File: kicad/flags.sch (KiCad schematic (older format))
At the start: 3 parts, among them U48 74LS173

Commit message: bugfixed design
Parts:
- renumbered U48 to U47
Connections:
- wire segments 27 -> 24
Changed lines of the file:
@@
 LIBS:valves
 LIBS:switches
-LIBS:74xxx
-LIBS:28c16
 LIBS:sap-be-cache
-EELAYER 24 0
+EELAYER 25 0
 EELAYER END
 $Descr A4 11693 8268
@@
 ZF
 $Comp
-L 74LS173 U48
+L 74LS173 U47
 U 1 1 5AD47646
 P 3600 2050
-F 0 "U48" H 3700 2150 50  0000 C CNN
+F 0 "U47" H 3700 2150 50  0000 C CNN
 F 1 "74LS173" H 3700 2000 50  0000 C CNN
 F 2 "" H 3600 2050 50  0000 C CNN
@@
 ~LOAD
 $Comp
-L GND #PWR090
+L GND #PWR88
 U 1 1 5AD4767C
 P 2450 2100
-F 0 "#PWR090" H 2450 1850 50  0001 C CNN
+F 0 "#PWR88" H 2450 1850 50  0001 C CNN
 F 1 "GND" H 2450 1950 50  0000 C CNN
 F 2 "" H 2450 2100 50  0000 C CNN
@@
 	1550 950  1300 950
 Wire Wire Line
-	2550 2300 2800 2300
-Wire Wire Line
-	2800 2300 2900 2300
+	2550 2300 2900 2300
 Wire Wire Line
 	2800 2300 2800 2200
@@
 Connection ~ 2800 2300
 Wire Wire Line
-	2900 2050 2800 2050
-Wire Wire Line
-	2800 2050 2450 2050
+	2450 2050 2900 2050
 Wire Wire Line
 	2450 2050 2450 2100
@@
 $EndComp
 $Comp
-L GND #PWR091
+L GND #PWR89
 U 1 1 5AD4AD59
 P 5600 2100
-F 0 "#PWR091" H 5600 1850 50  0001 C CNN
+F 0 "#PWR89" H 5600 1850 50  0001 C CNN
 F 1 "GND" H 5600 1950 50  0000 C CNN
 F 2 "" H 5600 2100 50  0000 C CNN
@@
 	5600 2100 5600 2050
 Wire Wire Line
-	5450 2050 5600 2050
-Wire Wire Line
-	5600 2050 5750 2050
+	5450 2050 5750 2050
 Wire Wire Line
 	5450 2050 5450 1950

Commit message: design as built
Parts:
- D601: renamed from D68; footprint (none) -> LEDs:LED-5MM
- D602: renamed from D69; footprint (none) -> LEDs:LED-5MM
- U601: renamed from U47; footprint (none) -> Housings_DIP:DIP-16_W7.62mm_LongPads
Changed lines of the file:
@@
 LIBS:valves
 LIBS:switches
+LIBS:74xxx
+LIBS:28c16
+LIBS:ne556
 LIBS:sap-be-cache
 EELAYER 25 0
@@
 Sheet 12 12
 Title "Simple As Possible computer by Ben Eater"
-Date "2017-05-10"
-Rev "1"
+Date "2018-06-03"
+Rev "2"
 Comp "Schematic released as CC BY-SA"
 Comment1 "Schematic capture by Vincent Sanders"
@@
 ZF
 $Comp
-L 74LS173 U47
+L 74LS173 U601
 U 1 1 5AD47646
 P 3600 2050
-F 0 "U47" H 3700 2150 50  0000 C CNN
+F 0 "U601" H 3700 2150 50  0000 C CNN
 F 1 "74LS173" H 3700 2000 50  0000 C CNN
-F 2 "" H 3600 2050 50  0000 C CNN
+F 2 "Housings_DIP:DIP-16_W7.62mm_LongPads" H 3600 2050 50  0001 C CNN
 F 3 "" H 3600 2050 50  0000 C CNN
 	1    3600 2050
@@
 ~LOAD
 $Comp
-L GND #PWR88
+L GND #PWR034
 U 1 1 5AD4767C
 P 2450 2100
-F 0 "#PWR88" H 2450 1850 50  0001 C CNN
+F 0 "#PWR034" H 2450 1850 50  0001 C CNN
 F 1 "GND" H 2450 1950 50  0000 C CNN
 F 2 "" H 2450 2100 50  0000 C CNN
@@
 NoConn ~ 2900 1800
 $Comp
-L LED D68
+L LED D601
 U 1 1 5AD4AD3C
 P 5450 1800
-F 0 "D68" H 5450 1900 50  0000 C CNN
+F 0 "D601" H 5450 1900 50  0000 C CNN
 F 1 "LED" H 5450 1700 50  0000 C CNN
-F 2 "" H 5450 1800 50  0000 C CNN
+F 2 "LEDs:LED-5MM" H 5450 1800 50  0001 C CNN
 F 3 "" H 5450 1800 50  0000 C CNN
 	1    5450 1800
@@
 $EndComp
 $Comp
-L LED D69
+L LED D602
 U 1 1 5AD4AD4E
 P 5750 1800
-F 0 "D69" H 5750 1900 50  0000 C CNN
+F 0 "D602" H 5750 1900 50  0000 C CNN
 F 1 "LED" H 5750 1700 50  0000 C CNN
-F 2 "" H 5750 1800 50  0000 C CNN
+F 2 "LEDs:LED-5MM" H 5750 1800 50  0001 C CNN
 F 3 "" H 5750 1800 50  0000 C CNN
 	1    5750 1800
@@
 $EndComp
 $Comp
-L GND #PWR89
+L GND #PWR035
 U 1 1 5AD4AD59
 P 5600 2100
-F 0 "#PWR89" H 5600 1850 50  0001 C CNN
+F 0 "#PWR035" H 5600 1850 50  0001 C CNN
 F 1 "GND" H 5600 1950 50  0000 C CNN
 F 2 "" H 5600 2100 50  0000 C CNN

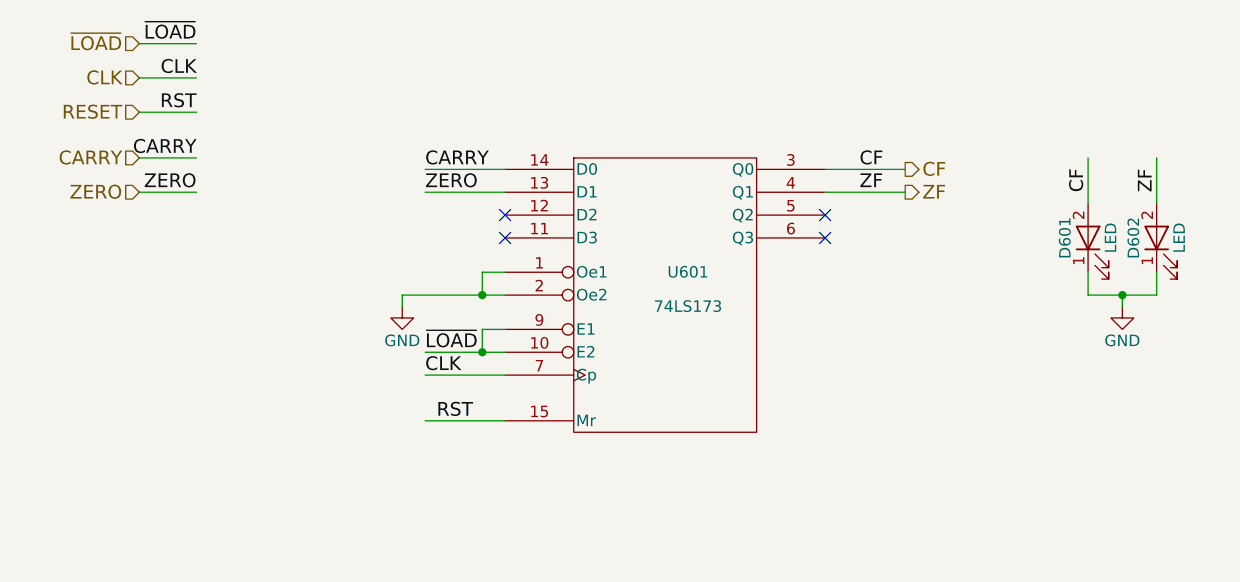
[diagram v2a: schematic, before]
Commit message: Update to current kicad version
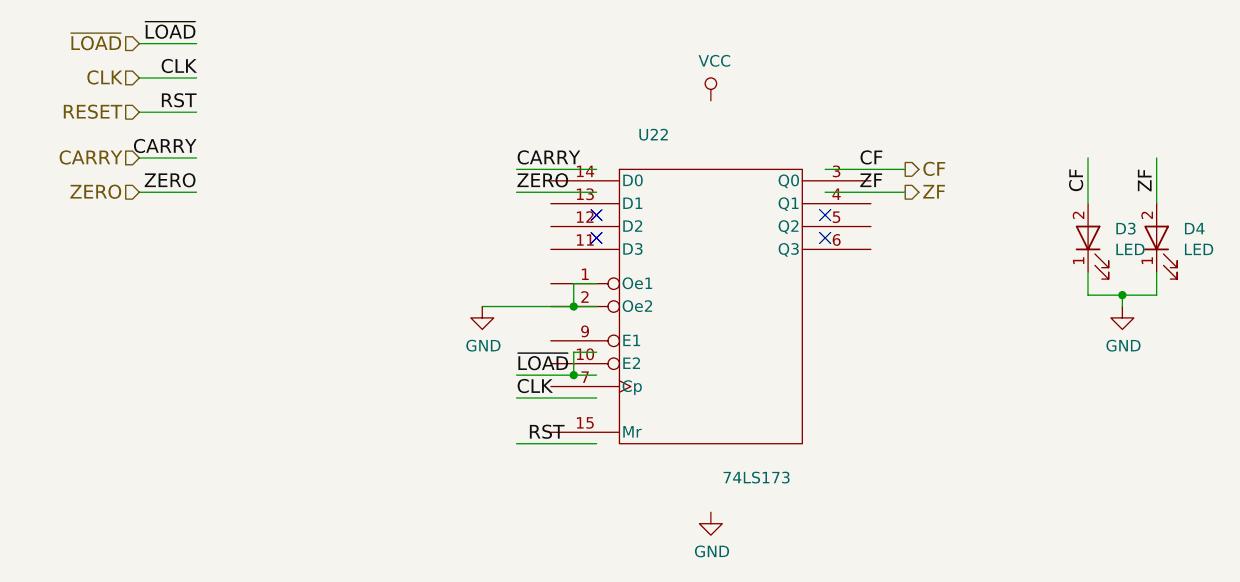
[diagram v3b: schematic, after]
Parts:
- removed D601, D602: LED, LEDs:LED-5MM, symbol LED
- removed U601: 74LS173, Housings_DIP:DIP-16_W7.62mm_LongPads, symbol 74LS173
- added D3, D4: LED, symbol Device:LED
- added U22: 74LS173, symbol 74xx:74LS173
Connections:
- net labels added: VCC
- wire segments 24 -> 26
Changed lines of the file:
@@
-EESchema Schematic File Version 2
-LIBS:power
-LIBS:device
-LIBS:transistors
-LIBS:conn
-LIBS:linear
-LIBS:regul
-LIBS:74xx
-LIBS:cmos4000
-LIBS:adc-dac
-LIBS:memory
-LIBS:xilinx
-LIBS:microcontrollers
-LIBS:dsp
-LIBS:microchip
-LIBS:analog_switches
-LIBS:motorola
-LIBS:texas
-LIBS:intel
-LIBS:audio
-LIBS:interface
-LIBS:digital-audio
-LIBS:philips
-LIBS:display
-LIBS:cypress
-LIBS:siliconi
-LIBS:opto
-LIBS:atmel
-LIBS:contrib
-LIBS:valves
-LIBS:switches
-LIBS:74xxx
-LIBS:28c16
-LIBS:ne556
-LIBS:sap-be-cache
-EELAYER 25 0
+EESchema Schematic File Version 4
+EELAYER 30 0
 EELAYER END
 $Descr A4 11693 8268
 encoding utf-8
-Sheet 12 12
-Title "Simple As Possible computer by Ben Eater"
-Date "2018-06-03"
-Rev "2"
+Sheet 7 13
+Title "Simple As Possible computer"
+Date "2017-05-10"
+Rev "1"
 Comp "Schematic released as CC BY-SA"
-Comment1 "Schematic capture by Vincent Sanders"
+Comment1 "This version by Vincent Sanders based on design by Ben Eater"
 Comment2 "Flags register"
 Comment3 ""
@@
 Text HLabel 4650 1600 2    60   Output ~ 0
 ZF
-$Comp
-L 74LS173 U601
-U 1 1 5AD47646
-P 3600 2050
-F 0 "U601" H 3700 2150 50  0000 C CNN
-F 1 "74LS173" H 3700 2000 50  0000 C CNN
-F 2 "Housings_DIP:DIP-16_W7.62mm_LongPads" H 3600 2050 50  0001 C CNN
-F 3 "" H 3600 2050 50  0000 C CNN
-	1    3600 2050
-	1    0    0    -1
-$EndComp
 Text Label 1550 950  2    60   ~ 0
 ~LOAD
-Text Label 2550 2300 0    60   ~ 0
+Text Label 2950 2400 0    60   ~ 0
 ~LOAD
-$Comp
-L GND #PWR034
-U 1 1 5AD4767C
-P 2450 2100
-F 0 "#PWR034" H 2450 1850 50  0001 C CNN
-F 1 "GND" H 2450 1950 50  0000 C CNN
-F 2 "" H 2450 2100 50  0000 C CNN
-F 3 "" H 2450 2100 50  0000 C CNN
-	1    2450 2100
-	1    0    0    -1
-$EndComp
-Text Label 2550 1500 0    60   ~ 0
+Text Label 2950 1500 0    60   ~ 0
 CARRY
-Text Label 2550 1600 0    60   ~ 0
+Text Label 2950 1600 0    60   ~ 0
 ZERO
 Text Label 1550 1450 2    60   ~ 0
@@
 Text Label 1550 1250 2    60   ~ 0
 RST
-Text Label 2600 2600 0    60   ~ 0
+Text Label 3000 2700 0    60   ~ 0
 RST
 Wire Wire Line
 	1550 950  1300 950
 Wire Wire Line
-	2550 2300 2900 2300
+	2950 2400 3200 2400
 Wire Wire Line
-	2800 2300 2800 2200
+	3200 2400 3300 2400
 Wire Wire Line
-	2800 2200 2900 2200
-Connection ~ 2800 2300
+	3200 2400 3200 2300
 Wire Wire Line
-	2450 2050 2900 2050
+	3200 2300 3300 2300
+Connection ~ 3200 2400
 Wire Wire Line
-	2450 2050 2450 2100
+	3300 2100 3200 2100
 Wire Wire Line
-	2900 1950 2800 1950
+	3300 2000 3200 2000
 Wire Wire Line
-	2800 1950 2800 2050
-Connection ~ 2800 2050
+	3200 2000 3200 2100
+Connection ~ 3200 2100
 Wire Wire Line
-	2550 1500 2900 1500
+	2950 1500 3300 1500
 Wire Wire Line
-	2550 1600 2900 1600
+	2950 1600 3300 1600
 Wire Wire Line
 	1550 1450 1300 1450
@@
 	1550 1100 1300 1100
 Wire Wire Line
-	2550 2600 2900 2600
+	2950 2700 3300 2700
 Wire Wire Line
-	2550 2400 2900 2400
-Text Label 2550 2400 0    60   ~ 0
+	2950 2500 3300 2500
+Text Label 2950 2500 0    60   ~ 0
 CLK
 Text Label 4450 1500 0    60   ~ 0
@@
 NoConn ~ 4300 1700
 NoConn ~ 4300 1800
-NoConn ~ 2900 1700
-NoConn ~ 2900 1800
-$Comp
-L LED D601
-U 1 1 5AD4AD3C
-P 5450 1800
-F 0 "D601" H 5450 1900 50  0000 C CNN
-F 1 "LED" H 5450 1700 50  0000 C CNN
-F 2 "LEDs:LED-5MM" H 5450 1800 50  0001 C CNN
-F 3 "" H 5450 1800 50  0000 C CNN
-	1    5450 1800
-	0    -1   -1   0
-$EndComp
-$Comp
-L LED D602
-U 1 1 5AD4AD4E
-P 5750 1800
-F 0 "D602" H 5750 1900 50  0000 C CNN
-F 1 "LED" H 5750 1700 50  0000 C CNN
-F 2 "LEDs:LED-5MM" H 5750 1800 50  0001 C CNN
-F 3 "" H 5750 1800 50  0000 C CNN
-	1    5750 1800
-	0    -1   -1   0
-$EndComp
-$Comp
-L GND #PWR035
-U 1 1 5AD4AD59
-P 5600 2100
-F 0 "#PWR035" H 5600 1850 50  0001 C CNN
-F 1 "GND" H 5600 1950 50  0000 C CNN
-F 2 "" H 5600 2100 50  0000 C CNN
-F 3 "" H 5600 2100 50  0000 C CNN
-	1    5600 2100
-	1    0    0    -1
-$EndComp
+NoConn ~ 3300 1700
+NoConn ~ 3300 1800
 Wire Wire Line
 	5600 2100 5600 2050
 Wire Wire Line
-	5450 2050 5750 2050
+	5450 2050 5600 2050
+Wire Wire Line
+	5600 2050 5750 2050
 Wire Wire Line
 	5450 2050 5450 1950
@@
 Text Label 5750 1600 1    60   ~ 0
 ZF
+$Comp
+L power:GND #PWR071
+U 1 1 5EA8388C
+P 2800 2100
+F 0 "#PWR071" H 2800 1850 50  0001 C CNN
+F 1 "GND" H 2805 1927 50  0000 C CNN
+F 2 "" H 2800 2100 50  0001 C CNN
+F 3 "" H 2800 2100 50  0001 C CNN
+	1    2800 2100
+	1    0    0    -1
+$EndComp
+Wire Wire Line
+	2800 2100 3200 2100
+$Comp
+L power:GND #PWR074
+U 1 1 5EA8545C
+P 5600 2100
+F 0 "#PWR074" H 5600 1850 50  0001 C CNN
+F 1 "GND" H 5605 1927 50  0000 C CNN
+F 2 "" H 5600 2100 50  0001 C CNN
+F 3 "" H 5600 2100 50  0001 C CNN
+	1    5600 2100
+	1    0    0    -1
+$EndComp
+$Comp
+L Device:LED D3
+U 1 1 5EA85B93
+P 5450 1800
+F 0 "D3" V 5489 1683 50  0000 R CNN
+F 1 "LED" V 5398 1683 50  0000 R CNN
+F 2 "" H 5450 1800 50  0001 C CNN
+F 3 "~" H 5450 1800 50  0001 C CNN
+	1    5450 1800
+	0    -1   -1   0
+$EndComp
+$Comp
+L Device:LED D4
+U 1 1 5EA8646D
+P 5750 1800
+F 0 "D4" V 5789 1683 50  0000 R CNN
+F 1 "LED" V 5698 1683 50  0000 R CNN
+F 2 "" H 5750 1800 50  0001 C CNN
+F 3 "~" H 5750 1800 50  0001 C CNN
+	1    5750 1800
+	0    -1   -1   0
+$EndComp
+$Comp
+L 74xx:74LS173 U22
+U 1 1 5EA87D23
+P 3800 2100
+F 0 "U22" H 3550 2850 50  0000 C CNN
+F 1 "74LS173" H 4000 1350 50  0000 C CNN
+F 2 "" H 3800 2100 50  0001 C CNN
+F 3 "http://www.ti.com/lit/gpn/sn74LS173" H 3800 2100 50  0001 C CNN
+	1    3800 2100
+	1    0    0    -1
+$EndComp
+$Comp
+L power:GND #PWR073
+U 1 1 5EA8EB64
+P 3800 3000
+F 0 "#PWR073" H 3800 2750 50  0001 C CNN
+F 1 "GND" H 3805 2827 50  0000 C CNN
+F 2 "" H 3800 3000 50  0001 C CNN
+F 3 "" H 3800 3000 50  0001 C CNN
+	1    3800 3000
+	1    0    0    -1
+$EndComp
+$Comp
+L power:VCC #PWR072
+U 1 1 5EA8F117
+P 3800 1200
+F 0 "#PWR072" H 3800 1050 50  0001 C CNN
+F 1 "VCC" H 3817 1373 50  0000 C CNN
+F 2 "" H 3800 1200 50  0001 C CNN
+F 3 "" H 3800 1200 50  0001 C CNN
+	1    3800 1200
+	1    0    0    -1
+$EndComp
 $EndSCHEMATC
